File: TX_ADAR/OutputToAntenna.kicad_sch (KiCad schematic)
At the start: 8 parts, among them J10 Conn_Coaxial, J3 Conn_Coaxial, J4 Conn_Coaxial, J5 Conn_Coaxial, J6 Conn_Coaxial, J7 Conn_Coaxial, J8 Conn_Coaxial, J9 Conn_Coaxial

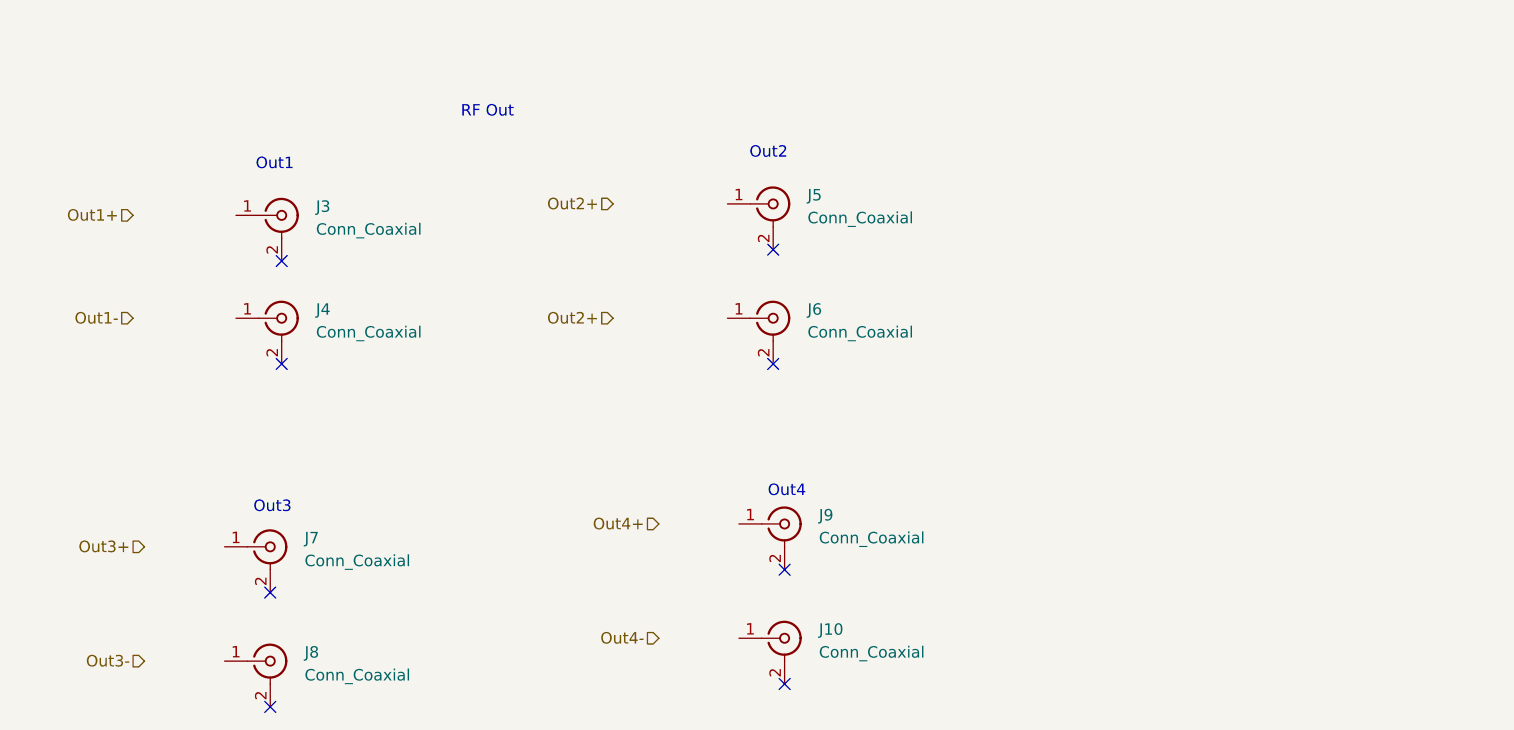
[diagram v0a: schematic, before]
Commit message: After Vccb>Vcca
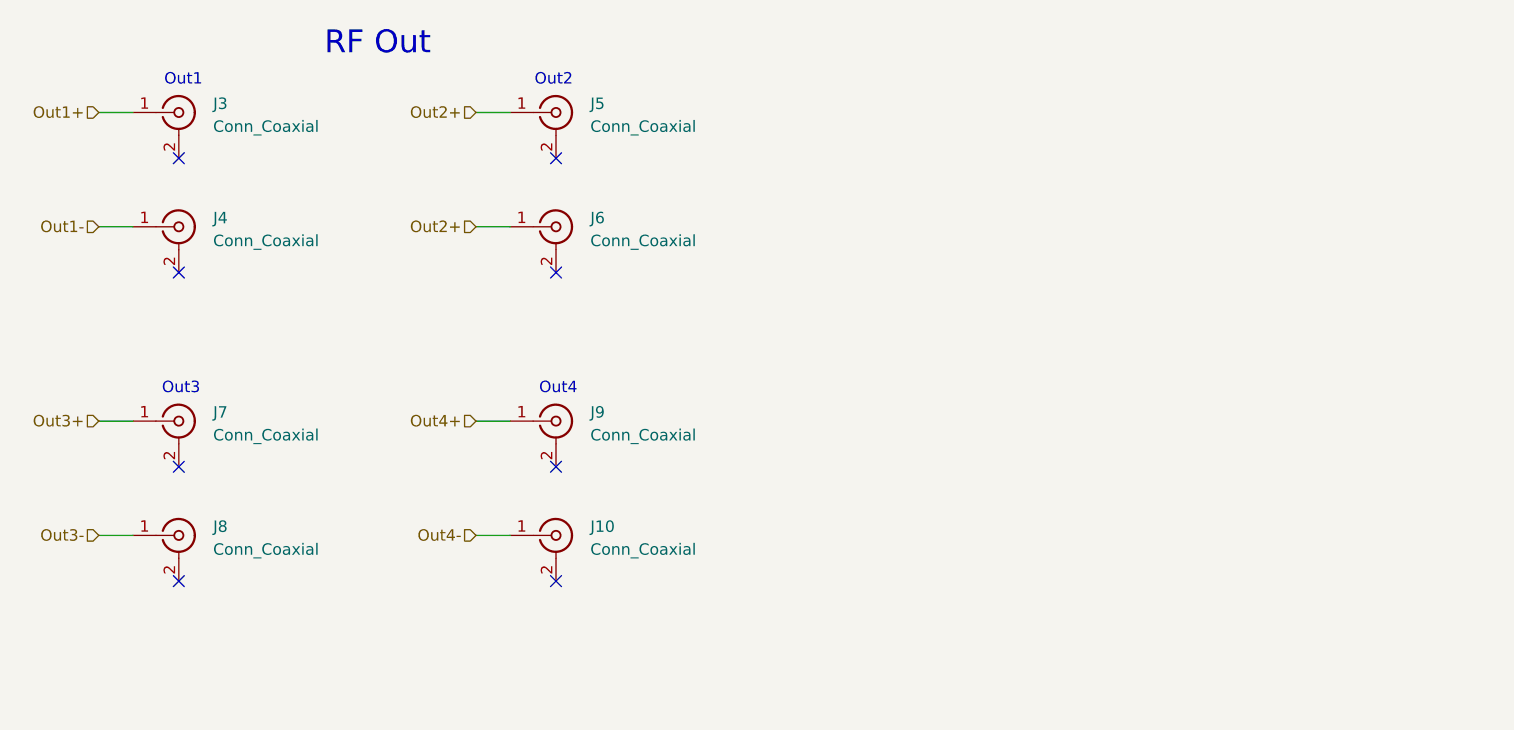
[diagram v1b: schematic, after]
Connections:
- net Out1+: now also J3.1 (In)
- net Out1-: now also J4.1 (In)
- net Out2+: now also J5.1 (In), J6.1 (In)
- net Out3+: now also J7.1 (In)
- net Out3-: now also J8.1 (In)
- net Out4+: now also J9.1 (In)
- net Out4-: now also J10.1 (In)
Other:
- moved on the sheet: J10, J3, J4, J5, J6, J7, J8, J9

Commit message: Moving things around
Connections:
- net Out2+: no longer J6.1 (In)
- new net Out2-: J6.1 (In)
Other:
- moved on the sheet: J10, J7, J8, J9
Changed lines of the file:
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@@
 	(text "Out4"
 		(exclude_from_sim no)
-		(at 73.914 54.864 0)
+		(at 156.464 20.574 0)
 		(effects
 			(font
@@
 	(text "Out3"
 		(exclude_from_sim no)
-		(at 32.004 54.864 0)
+		(at 114.554 20.574 0)
 		(effects
 			(font
@@
 	(text "RF Out"
 		(exclude_from_sim no)
-		(at 53.848 16.51 0)
+		(at 94.742 16.51 0)
 		(effects
 			(font
@@
 	)
 	(no_connect
-		(at 31.75 76.2)
+		(at 114.3 41.91)
 	)
 	(no_connect
-		(at 73.66 63.5)
+		(at 156.21 29.21)
 	)
 	(no_connect
@@
 	)
 	(no_connect
-		(at 31.75 63.5)
+		(at 114.3 29.21)
 	)
 	(no_connect
-		(at 73.66 76.2)
+		(at 156.21 41.91)
 	)
 	(wire
 		(pts
-			(xy 22.86 58.42) (xy 26.67 58.42)
+			(xy 105.41 24.13) (xy 109.22 24.13)
 		)
 		(stroke
@@
 	(wire
 		(pts
-			(xy 64.77 58.42) (xy 68.58 58.42)
+			(xy 147.32 24.13) (xy 151.13 24.13)
 		)
 		(stroke
@@
 	(wire
 		(pts
-			(xy 22.86 71.12) (xy 26.67 71.12)
+			(xy 105.41 36.83) (xy 109.22 36.83)
 		)
 		(stroke
@@
 	(wire
 		(pts
-			(xy 64.77 71.12) (xy 68.58 71.12)
+			(xy 147.32 36.83) (xy 151.13 36.83)
 		)
 		(stroke
@@
 	(hierarchical_label "Out4-"
 		(shape input)
-		(at 64.77 71.12 180)
+		(at 147.32 36.83 180)
 		(effects
 			(font
@@
 	(hierarchical_label "Out4+"
 		(shape input)
-		(at 64.77 58.42 180)
+		(at 147.32 24.13 180)
 		(effects
 			(font
@@
 	(hierarchical_label "Out3+"
 		(shape input)
-		(at 22.86 58.42 180)
+		(at 105.41 24.13 180)
 		(effects
 			(font
@@
 		)
 	)
-	(hierarchical_label "Out2+"
+	(hierarchical_label "Out2-"
 		(shape input)
 		(at 64.77 36.83 180)
@@
 	(hierarchical_label "Out3-"
 		(shape input)
-		(at 22.86 71.12 180)
+		(at 105.41 36.83 180)
 		(effects
 			(font
@@
 	(symbol
 		(lib_id "Connector:Conn_Coaxial")
-		(at 73.66 71.12 0)
+		(at 156.21 36.83 0)
 		(unit 1)
 		(body_style 1)
@@
 		(fields_autoplaced yes)
 		(property "Reference" "J10"
-			(at 77.47 70.1431 0)
+			(at 160.02 35.8531 0)
 			(show_name no)
 			(do_not_autoplace no)
@@
 		)
 		(property "Value" "Conn_Coaxial"
-			(at 77.47 72.6831 0)
+			(at 160.02 38.3931 0)
 			(show_name no)
 			(do_not_autoplace no)
@@
 		)
 		(property "Footprint" ""
-			(at 73.66 71.12 0)
+			(at 156.21 36.83 0)
 			(hide yes)
 			(show_name no)
@@
 		)
 		(property "Datasheet" ""
-			(at 73.66 71.12 0)
+			(at 156.21 36.83 0)
 			(hide yes)
 			(show_name no)
@@
 		)
 		(property "Description" "coaxial connector (BNC, SMA, SMB, SMC, Cinch/RCA, LEMO, ...)"
-			(at 73.66 71.12 0)
+			(at 156.21 36.83 0)
 			(hide yes)
 			(show_name no)
@@
 	(symbol
 		(lib_id "Connector:Conn_Coaxial")
-		(at 73.66 58.42 0)
+		(at 156.21 24.13 0)
 		(unit 1)
 		(body_style 1)
@@
 		(fields_autoplaced yes)
 		(property "Reference" "J9"
-			(at 77.47 57.4431 0)
+			(at 160.02 23.1531 0)
 			(show_name no)
 			(do_not_autoplace no)
@@
 		)
 		(property "Value" "Conn_Coaxial"
-			(at 77.47 59.9831 0)
+			(at 160.02 25.6931 0)
 			(show_name no)
 			(do_not_autoplace no)
@@
 		)
 		(property "Footprint" ""
-			(at 73.66 58.42 0)
+			(at 156.21 24.13 0)
 			(hide yes)
 			(show_name no)
@@
 		)
 		(property "Datasheet" ""
-			(at 73.66 58.42 0)
+			(at 156.21 24.13 0)
 			(hide yes)
 			(show_name no)
@@
 		)
 		(property "Description" "coaxial connector (BNC, SMA, SMB, SMC, Cinch/RCA, LEMO, ...)"
-			(at 73.66 58.42 0)
+			(at 156.21 24.13 0)
 			(hide yes)
 			(show_name no)
@@
 	(symbol
 		(lib_id "Connector:Conn_Coaxial")
-		(at 31.75 71.12 0)
+		(at 114.3 36.83 0)
 		(unit 1)
 		(body_style 1)
@@
 		(fields_autoplaced yes)
 		(property "Reference" "J8"
-			(at 35.56 70.1431 0)
+			(at 118.11 35.8531 0)
 			(show_name no)
 			(do_not_autoplace no)
@@
 		)
 		(property "Value" "Conn_Coaxial"
-			(at 35.56 72.6831 0)
+			(at 118.11 38.3931 0)
 			(show_name no)
 			(do_not_autoplace no)
@@
 		)
 		(property "Footprint" ""
-			(at 31.75 71.12 0)
+			(at 114.3 36.83 0)
 			(hide yes)
 			(show_name no)
@@
 		)
 		(property "Datasheet" ""
-			(at 31.75 71.12 0)
+			(at 114.3 36.83 0)
 			(hide yes)
 			(show_name no)
@@
 		)
 		(property "Description" "coaxial connector (BNC, SMA, SMB, SMC, Cinch/RCA, LEMO, ...)"
-			(at 31.75 71.12 0)
+			(at 114.3 36.83 0)
 			(hide yes)
 			(show_name no)
@@
 	(symbol
 		(lib_id "Connector:Conn_Coaxial")
-		(at 31.75 58.42 0)
+		(at 114.3 24.13 0)
 		(unit 1)
 		(body_style 1)
@@
 		(fields_autoplaced yes)
 		(property "Reference" "J7"
-			(at 35.56 57.4431 0)
+			(at 118.11 23.1531 0)
 			(show_name no)
 			(do_not_autoplace no)
@@
 		)
 		(property "Value" "Conn_Coaxial"
-			(at 35.56 59.9831 0)
+			(at 118.11 25.6931 0)
 			(show_name no)
 			(do_not_autoplace no)
@@
 		)
 		(property "Footprint" ""
-			(at 31.75 58.42 0)
+			(at 114.3 24.13 0)
 			(hide yes)
 			(show_name no)
@@
 		)
 		(property "Datasheet" ""
-			(at 31.75 58.42 0)
+			(at 114.3 24.13 0)
 			(hide yes)
 			(show_name no)
@@
 		)
 		(property "Description" "coaxial connector (BNC, SMA, SMB, SMC, Cinch/RCA, LEMO, ...)"
-			(at 31.75 58.42 0)
-			(hide yes)
-			(show_name no)
+			(at 114.3 24.13 0)
+			(hide yes)
+			(show_name no)

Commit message: Fixing problems pointed out
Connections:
- net GND: now reaches J10.2 (Ext)
- net GND: now also J3.2 (Ext), J4.2 (Ext), J5.2 (Ext), J6.2 (Ext), J7.2 (Ext), J8.2 (Ext), J9.2 (Ext)
- no-connect marks 8 -> 0
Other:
- moved on the sheet: J10, J4, J6, J8

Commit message: Fixed more issues
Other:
- note added: "All eight lines must have equal electrical and mechanical lengths"
- moved on the sheet: J10, J3, J4, J5, J6, J7, J8, J9

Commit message: Got footprints to work
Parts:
- J10, J3, J4, J5, J6, J7, J8, J9: footprint (none) -> 142_1701_831:BEL_142-1701-831
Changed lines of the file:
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@@
 			)
 		)
-		(property "Footprint" ""
+		(property "Footprint" "142_1701_831:BEL_142-1701-831"
 			(at 158.75 49.53 0)
 			(hide yes)
@@
 			)
 		)
-		(property "Footprint" ""
+		(property "Footprint" "142_1701_831:BEL_142-1701-831"
 			(at 158.75 30.48 0)
 			(hide yes)
@@
 			)
 		)
-		(property "Footprint" ""
+		(property "Footprint" "142_1701_831:BEL_142-1701-831"
 			(at 116.84 49.53 0)
 			(hide yes)
@@
 			)
 		)
-		(property "Footprint" ""
+		(property "Footprint" "142_1701_831:BEL_142-1701-831"
 			(at 34.29 49.53 0)
 			(hide yes)
@@
 			)
 		)
-		(property "Footprint" ""
+		(property "Footprint" "142_1701_831:BEL_142-1701-831"
 			(at 76.2 30.48 0)
 			(hide yes)
@@
 			)
 		)
-		(property "Footprint" ""
+		(property "Footprint" "142_1701_831:BEL_142-1701-831"
 			(at 34.29 30.48 0)
 			(hide yes)
@@
 			)
 		)
-		(property "Footprint" ""
+		(property "Footprint" "142_1701_831:BEL_142-1701-831"
 			(at 116.84 30.48 0)
 			(hide yes)
@@
 			)
 		)
-		(property "Footprint" ""
+		(property "Footprint" "142_1701_831:BEL_142-1701-831"
 			(at 76.2 49.53 0)
 			(hide yes)

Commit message: Layout updates
Using vias to connect hard to reach spots
Added copper pours
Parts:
- J10, J3, J4, J5, J6, J7, J8, J9: footprint 142_1701_831:BEL_142-1701-831 -> CON292001_1:TE_CON292001-1
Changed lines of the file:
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@@
 			)
 		)
-		(property "Footprint" "142_1701_831:BEL_142-1701-831"
+		(property "Footprint" "CON292001_1:TE_CON292001-1"
 			(at 158.75 49.53 0)
 			(hide yes)
@@
 			)
 		)
-		(property "Footprint" "142_1701_831:BEL_142-1701-831"
+		(property "Footprint" "CON292001_1:TE_CON292001-1"
 			(at 158.75 30.48 0)
 			(hide yes)
@@
 			)
 		)
-		(property "Footprint" "142_1701_831:BEL_142-1701-831"
+		(property "Footprint" "CON292001_1:TE_CON292001-1"
 			(at 116.84 49.53 0)
 			(hide yes)
@@
 			)
 		)
-		(property "Footprint" "142_1701_831:BEL_142-1701-831"
+		(property "Footprint" "CON292001_1:TE_CON292001-1"
 			(at 34.29 49.53 0)
 			(hide yes)
@@
 			)
 		)
-		(property "Footprint" "142_1701_831:BEL_142-1701-831"
+		(property "Footprint" "CON292001_1:TE_CON292001-1"
 			(at 76.2 30.48 0)
 			(hide yes)
@@
 			)
 		)
-		(property "Footprint" "142_1701_831:BEL_142-1701-831"
+		(property "Footprint" "CON292001_1:TE_CON292001-1"
 			(at 34.29 30.48 0)
 			(hide yes)
@@
 			)
 		)
-		(property "Footprint" "142_1701_831:BEL_142-1701-831"
+		(property "Footprint" "CON292001_1:TE_CON292001-1"
 			(at 116.84 30.48 0)
 			(hide yes)
@@
 			)
 		)
-		(property "Footprint" "142_1701_831:BEL_142-1701-831"
+		(property "Footprint" "CON292001_1:TE_CON292001-1"
 			(at 76.2 49.53 0)
 			(hide yes)

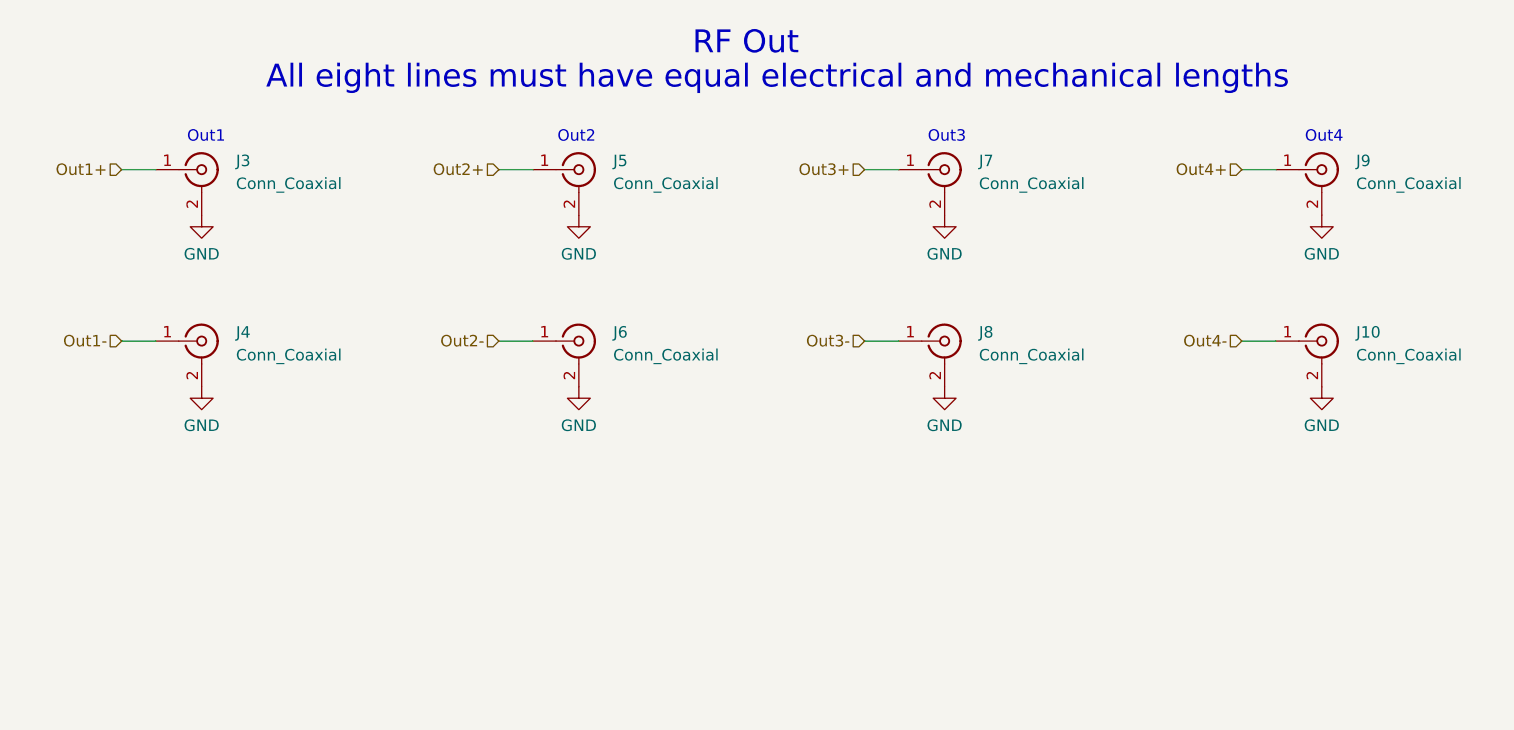
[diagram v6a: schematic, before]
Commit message: Updates to layout and connectors
**Need to add 50 ohm term to gnd from connector on positive outs for 2.92 vert launches**
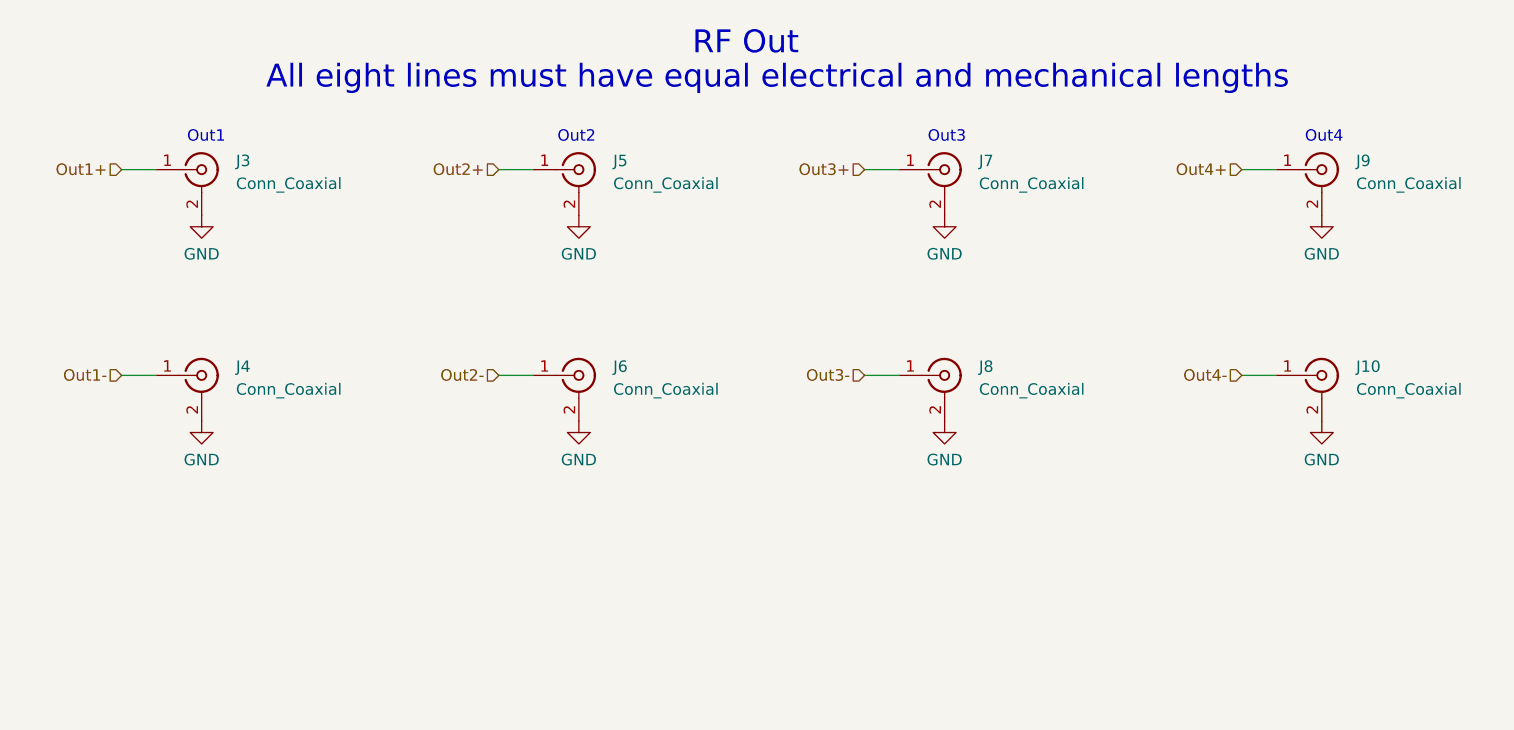
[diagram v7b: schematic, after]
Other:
- moved on the sheet: J10, J4, J6, J8

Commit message: Added Level Shifters
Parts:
- added R1, R4, R7, R8: 50, symbol Device:R_Small_US
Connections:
- net GND: now also R1.2, R4.2, R7.2, R8.2
- net Out1+: now also R8.1
- net Out2+: now also R1.1
- net Out3+: now also R4.1
- net Out4+: now also R7.1
